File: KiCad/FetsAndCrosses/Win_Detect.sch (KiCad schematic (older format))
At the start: 0 parts

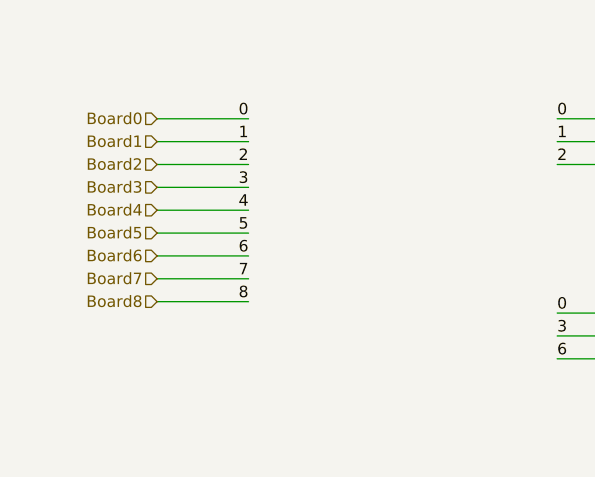
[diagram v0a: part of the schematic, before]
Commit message: Reworked everything to use Buses
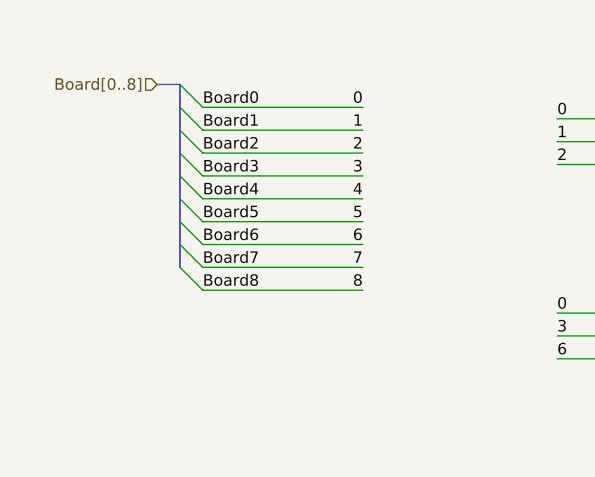
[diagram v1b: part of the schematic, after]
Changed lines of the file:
@@
 $Descr A4 11693 8268
 encoding utf-8
-Sheet 29 215
+Sheet 18 400
 Title ""
 Date ""
@@
 Wire Wire Line
 	6450 1350 6750 1350
-Text HLabel 1400 1350 0    50   Input ~ 0
-Board0
-Text HLabel 1400 1450 0    50   Input ~ 0
-Board1
-Text HLabel 1400 1550 0    50   Input ~ 0
-Board2
-Text HLabel 1400 1650 0    50   Input ~ 0
-Board3
-Text HLabel 1400 1750 0    50   Input ~ 0
-Board4
-Text HLabel 1400 1850 0    50   Input ~ 0
-Board5
-Text HLabel 1400 1950 0    50   Input ~ 0
-Board6
-Text HLabel 1400 2050 0    50   Input ~ 0
-Board7
-Text HLabel 1400 2150 0    50   Input ~ 0
-Board8
-Wire Wire Line
-	1400 1350 1800 1350
-Wire Wire Line
-	1400 1450 1800 1450
-Wire Wire Line
-	1400 1550 1800 1550
-Wire Wire Line
-	1400 1650 1800 1650
-Wire Wire Line
-	1400 1750 1800 1750
-Wire Wire Line
-	1400 1850 1800 1850
-Wire Wire Line
-	1400 1950 1800 1950
-Wire Wire Line
-	1400 2050 1800 2050
-Wire Wire Line
-	1400 2150 1800 2150
 $Sheet
 S 9000 1250 550  900
@@
 Text HLabel 10000 1700 2    50   Output ~ 0
 Is_Win
-Text Label 1800 1350 2    50   ~ 0
-0
-Text Label 1800 1450 2    50   ~ 0
-1
-Text Label 1800 1550 2    50   ~ 0
-2
-Text Label 1800 1650 2    50   ~ 0
-3
-Text Label 1800 1750 2    50   ~ 0
-4
-Text Label 1800 1850 2    50   ~ 0
-5
-Text Label 1800 1950 2    50   ~ 0
-6
-Text Label 1800 2050 2    50   ~ 0
-7
-Text Label 1800 2150 2    50   ~ 0
-8
 Text Label 3150 1350 0    50   ~ 0
 0
@@
 Text Notes 4000 1000 0    50   ~ 0
 Checks if a Player has won by AND-ing all Rows, Cols, and Diags individually
+Wire Wire Line
+	1600 2100 2300 2100
+Wire Wire Line
+	1600 2000 2300 2000
+Wire Wire Line
+	1600 1900 2300 1900
+Wire Wire Line
+	1600 1800 2300 1800
+Wire Wire Line
+	1600 1700 2300 1700
+Wire Wire Line
+	1600 1600 2300 1600
+Wire Wire Line
+	1600 1500 2300 1500
+Wire Wire Line
+	1600 1400 2300 1400
+Wire Wire Line
+	1600 1300 2300 1300
+Entry Wire Line
+	1500 2000 1600 2100
+Entry Wire Line
+	1500 1900 1600 2000
+Entry Wire Line
+	1500 1800 1600 1900
+Entry Wire Line
+	1500 1700 1600 1800
+Entry Wire Line
+	1500 1600 1600 1700
+Entry Wire Line
+	1500 1500 1600 1600
+Entry Wire Line
+	1500 1400 1600 1500
+Entry Wire Line
+	1500 1300 1600 1400
+Entry Wire Line
+	1500 1200 1600 1300
+Wire Bus Line
+	1400 1200 1500 1200
+Text Label 2300 2100 2    50   ~ 0
+8
+Text Label 2300 2000 2    50   ~ 0
+7
+Text Label 2300 1900 2    50   ~ 0
+6
+Text Label 2300 1800 2    50   ~ 0
+5
+Text Label 2300 1700 2    50   ~ 0
+4
+Text Label 2300 1600 2    50   ~ 0
+3
+Text Label 2300 1500 2    50   ~ 0
+2
+Text Label 2300 1400 2    50   ~ 0
+1
+Text Label 2300 1300 2    50   ~ 0
+0
+Text Label 1600 1300 0    50   ~ 0
+Board0
+Text Label 1600 1400 0    50   ~ 0
+Board1
+Text Label 1600 1500 0    50   ~ 0
+Board2
+Text Label 1600 1600 0    50   ~ 0
+Board3
+Text Label 1600 1700 0    50   ~ 0
+Board4
+Text Label 1600 1800 0    50   ~ 0
+Board5
+Text Label 1600 1900 0    50   ~ 0
+Board6
+Text Label 1600 2000 0    50   ~ 0
+Board7
+Text Label 1600 2100 0    50   ~ 0
+Board8
+Text HLabel 1400 1200 0    50   Input ~ 0
+Board[0..8]
+Wire Bus Line
+	1500 1200 1500 2000
 $EndSCHEMATC
